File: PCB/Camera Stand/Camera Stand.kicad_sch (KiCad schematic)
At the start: 6 parts, among them J2 HMC5883L, J3 Motor Drive, J4 Keypad 4x4, J9 GPS Module, M1 Motor_Servo, U1 NRF24L01

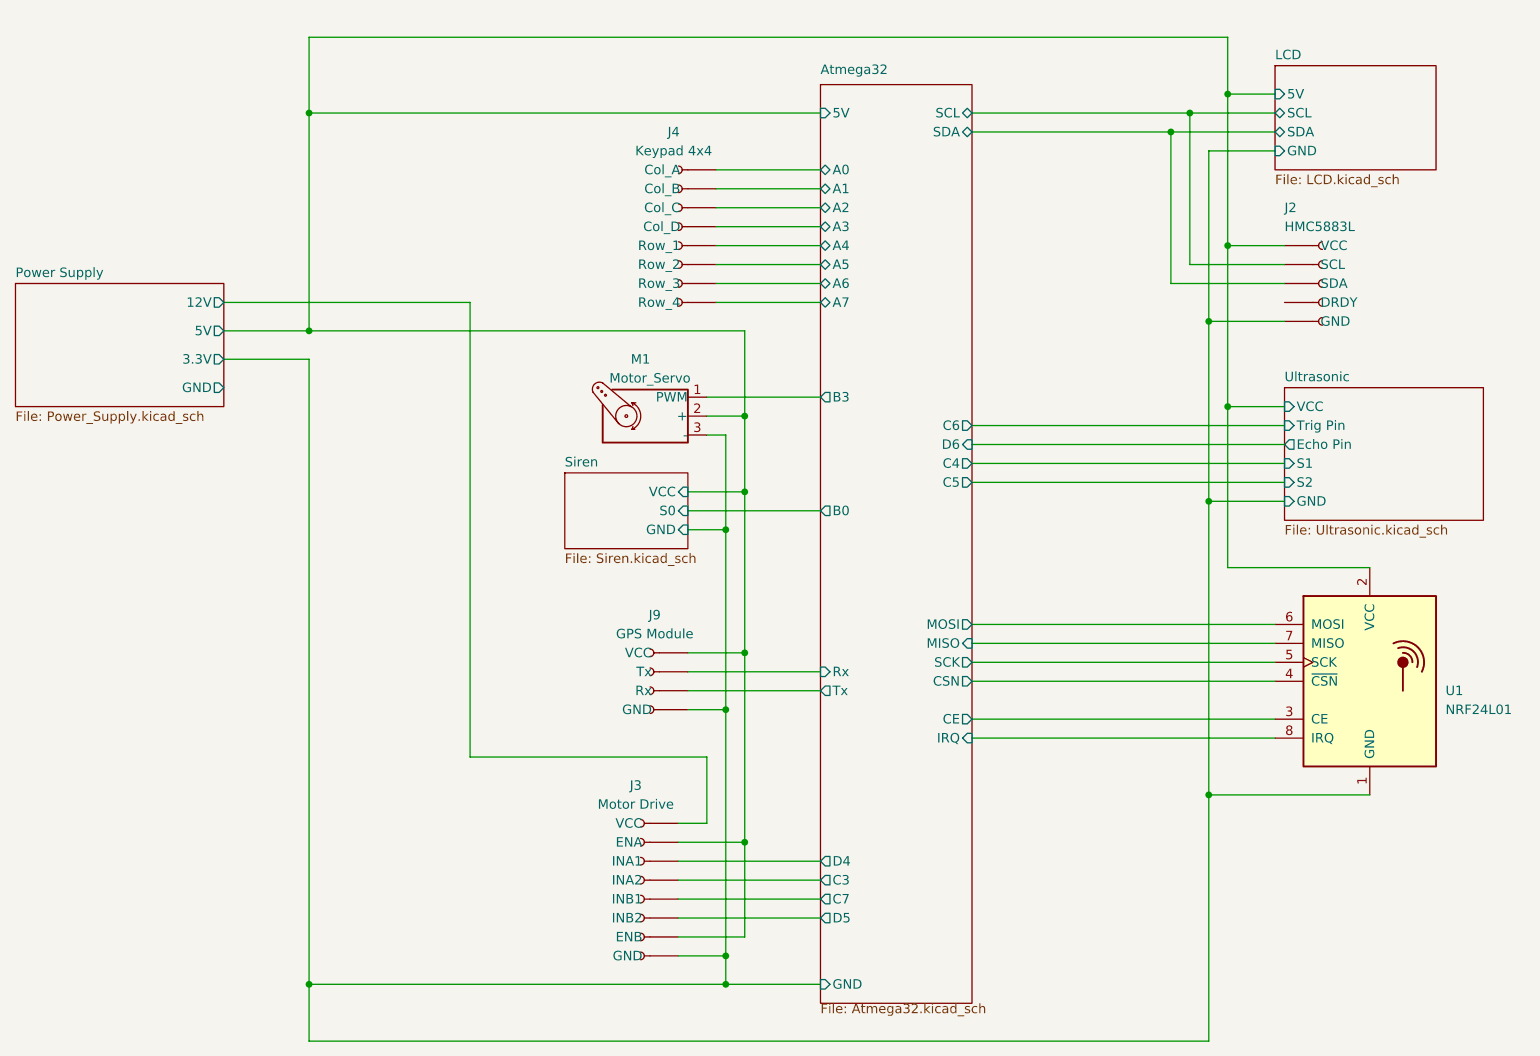
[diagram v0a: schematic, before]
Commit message: 3.3v error in PCB
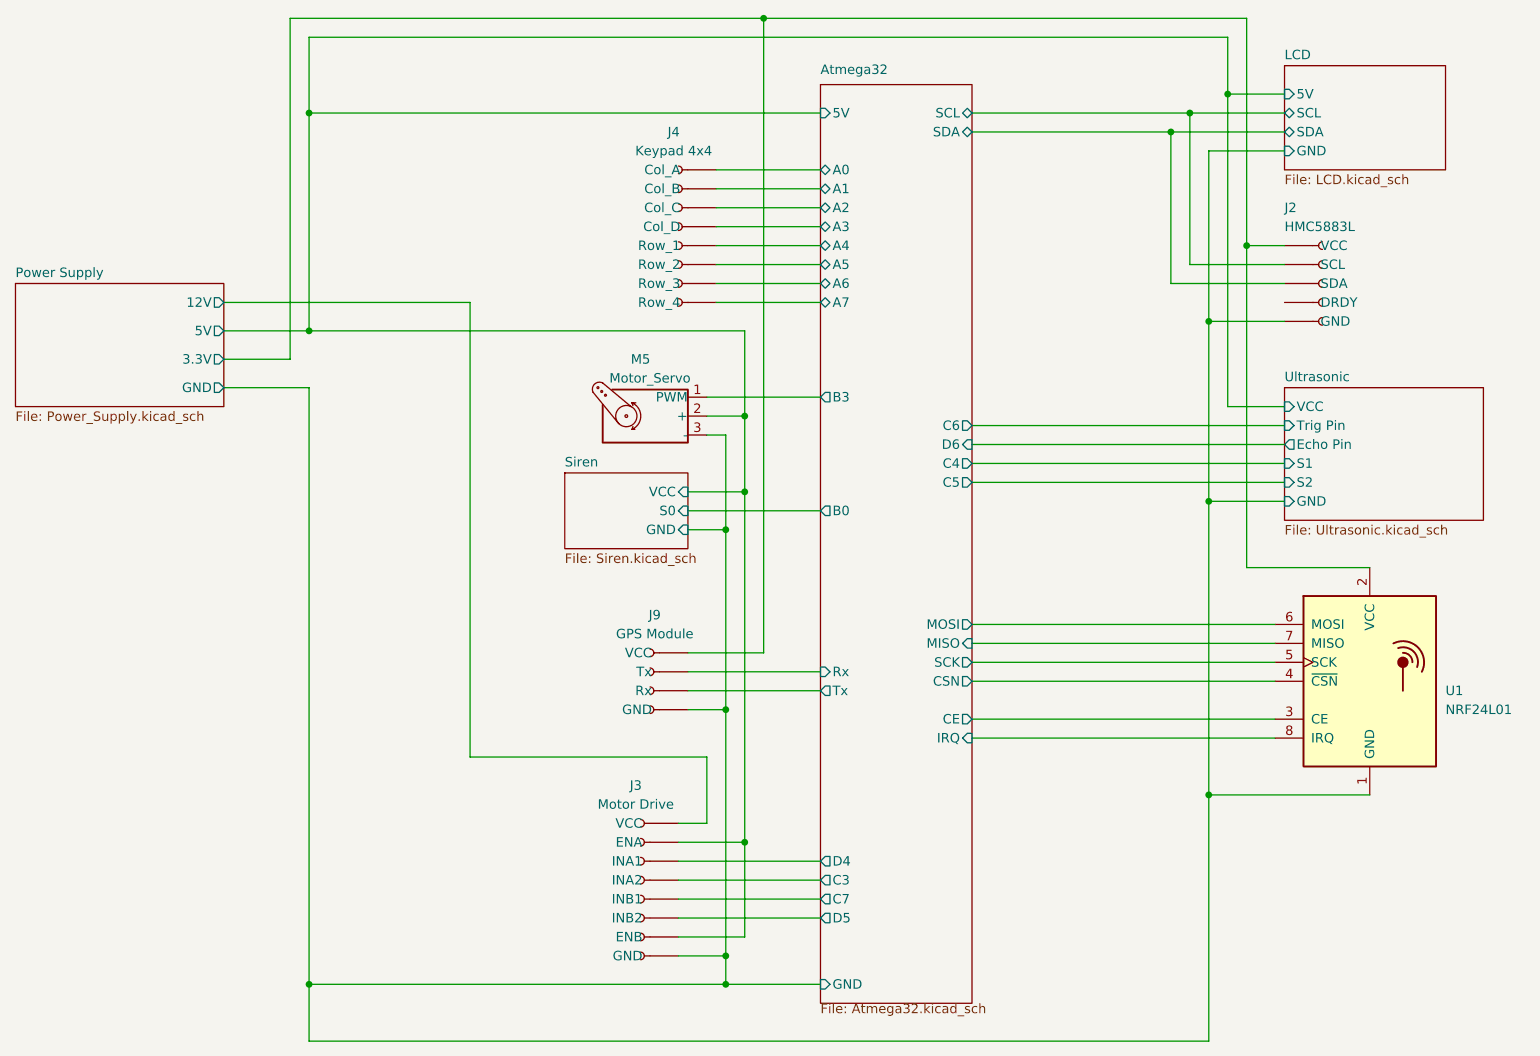
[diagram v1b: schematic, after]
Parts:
- renumbered M1 to M5
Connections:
- net Atmega32/5V: no longer J2.1 (VCC), J9.1 (VCC), U1.2 (VCC)
- new net Power Supply/3.3V: J2.1 (VCC), J9.1 (VCC), U1.2 (VCC)
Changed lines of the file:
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@@
   (junction (at 146.05 82.55) (diameter 0) (color 0 0 0 0)
   )
-  (junction (at 210.82 71.12) (diameter 0) (color 0 0 0 0)
-  )
   (junction (at 208.28 59.69) (diameter 0) (color 0 0 0 0)
   )
-  (junction (at 210.82 49.53) (diameter 0) (color 0 0 0 0)
-  )
-  (junction (at 146.05 104.14) (diameter 0) (color 0 0 0 0)
+  (junction (at 148.59 19.05) (diameter 0) (color 0 0 0 0)
   )
   (junction (at 87.63 148.59) (diameter 0) (color 0 0 0 0)
@@
   (junction (at 87.63 31.75) (diameter 0) (color 0 0 0 0)
   )
+  (junction (at 213.36 49.53) (diameter 0) (color 0 0 0 0)
+  )
   (junction (at 143.51 111.76) (diameter 0) (color 0 0 0 0)
   )
@@
     (stroke (width 0) (type default) (color 0 0 0 0))
   )
-  (wire (pts (xy 203.2 34.29) (xy 217.17 34.29))
+  (wire (pts (xy 203.2 34.29) (xy 218.44 34.29))
     (stroke (width 0) (type default) (color 0 0 0 0))
   )
@@
     (stroke (width 0) (type default) (color 0 0 0 0))
   )
-  (wire (pts (xy 208.28 36.83) (xy 217.17 36.83))
+  (wire (pts (xy 208.28 36.83) (xy 218.44 36.83))
     (stroke (width 0) (type default) (color 0 0 0 0))
   )
@@
     (stroke (width 0) (type default) (color 0 0 0 0))
   )
+  (wire (pts (xy 213.36 19.05) (xy 213.36 49.53))
+    (stroke (width 0) (type default) (color 0 0 0 0))
+  )
+  (wire (pts (xy 213.36 49.53) (xy 213.36 92.71))
+    (stroke (width 0) (type default) (color 0 0 0 0))
+  )
   (wire (pts (xy 208.28 123.19) (xy 208.28 83.82))
     (stroke (width 0) (type default) (color 0 0 0 0))
@@
     (stroke (width 0) (type default) (color 0 0 0 0))
   )
-  (wire (pts (xy 210.82 49.53) (xy 210.82 29.21))
+  (wire (pts (xy 210.82 29.21) (xy 210.82 71.12))
     (stroke (width 0) (type default) (color 0 0 0 0))
   )
@@
     (stroke (width 0) (type default) (color 0 0 0 0))
   )
-  (wire (pts (xy 76.2 64.77) (xy 87.63 64.77))
-    (stroke (width 0) (type default) (color 0 0 0 0))
-  )
   (wire (pts (xy 140.97 118.11) (xy 140.97 127))
     (stroke (width 0) (type default) (color 0 0 0 0))
@@
     (stroke (width 0) (type default) (color 0 0 0 0))
   )
-  (wire (pts (xy 146.05 82.55) (xy 146.05 104.14))
+  (wire (pts (xy 146.05 82.55) (xy 146.05 129.54))
     (stroke (width 0) (type default) (color 0 0 0 0))
   )
@@
     (stroke (width 0) (type default) (color 0 0 0 0))
   )
-  (wire (pts (xy 205.74 31.75) (xy 217.17 31.75))
+  (wire (pts (xy 87.63 68.58) (xy 87.63 148.59))
+    (stroke (width 0) (type default) (color 0 0 0 0))
+  )
+  (wire (pts (xy 205.74 31.75) (xy 218.44 31.75))
+    (stroke (width 0) (type default) (color 0 0 0 0))
+  )
+  (wire (pts (xy 148.59 19.05) (xy 148.59 104.14))
     (stroke (width 0) (type default) (color 0 0 0 0))
   )
@@
     (stroke (width 0) (type default) (color 0 0 0 0))
   )
+  (wire (pts (xy 76.2 64.77) (xy 85.09 64.77))
+    (stroke (width 0) (type default) (color 0 0 0 0))
+  )
   (wire (pts (xy 146.05 72.39) (xy 146.05 82.55))
     (stroke (width 0) (type default) (color 0 0 0 0))
@@
     (stroke (width 0) (type default) (color 0 0 0 0))
   )
-  (wire (pts (xy 210.82 71.12) (xy 210.82 92.71))
-    (stroke (width 0) (type default) (color 0 0 0 0))
-  )
   (wire (pts (xy 137.16 137.16) (xy 156.21 137.16))
     (stroke (width 0) (type default) (color 0 0 0 0))
   )
-  (wire (pts (xy 138.43 104.14) (xy 146.05 104.14))
+  (wire (pts (xy 138.43 104.14) (xy 148.59 104.14))
     (stroke (width 0) (type default) (color 0 0 0 0))
   )
@@
     (stroke (width 0) (type default) (color 0 0 0 0))
   )
+  (wire (pts (xy 85.09 19.05) (xy 148.59 19.05))
+    (stroke (width 0) (type default) (color 0 0 0 0))
+  )
   (wire (pts (xy 176.53 105.41) (xy 217.17 105.41))
     (stroke (width 0) (type default) (color 0 0 0 0))
@@
     (stroke (width 0) (type default) (color 0 0 0 0))
   )
-  (wire (pts (xy 229.87 92.71) (xy 210.82 92.71))
+  (wire (pts (xy 229.87 92.71) (xy 213.36 92.71))
     (stroke (width 0) (type default) (color 0 0 0 0))
   )
@@
     (stroke (width 0) (type default) (color 0 0 0 0))
   )
-  (wire (pts (xy 210.82 71.12) (xy 210.82 49.53))
-    (stroke (width 0) (type default) (color 0 0 0 0))
-  )
   (wire (pts (xy 176.53 76.2) (xy 218.44 76.2))
     (stroke (width 0) (type default) (color 0 0 0 0))
@@
     (stroke (width 0) (type default) (color 0 0 0 0))
   )
-  (wire (pts (xy 210.82 29.21) (xy 217.17 29.21))
+  (wire (pts (xy 210.82 29.21) (xy 218.44 29.21))
     (stroke (width 0) (type default) (color 0 0 0 0))
   )
@@
     (stroke (width 0) (type default) (color 0 0 0 0))
   )
+  (wire (pts (xy 148.59 19.05) (xy 213.36 19.05))
+    (stroke (width 0) (type default) (color 0 0 0 0))
+  )
+  (wire (pts (xy 85.09 64.77) (xy 85.09 19.05))
+    (stroke (width 0) (type default) (color 0 0 0 0))
+  )
   (wire (pts (xy 138.43 106.68) (xy 156.21 106.68))
     (stroke (width 0) (type default) (color 0 0 0 0))
   )
+  (wire (pts (xy 76.2 68.58) (xy 87.63 68.58))
+    (stroke (width 0) (type default) (color 0 0 0 0))
+  )
   (wire (pts (xy 143.51 144.78) (xy 143.51 148.59))
     (stroke (width 0) (type default) (color 0 0 0 0))
   )
-  (wire (pts (xy 218.44 49.53) (xy 210.82 49.53))
+  (wire (pts (xy 213.36 49.53) (xy 218.44 49.53))
     (stroke (width 0) (type default) (color 0 0 0 0))
   )
@@
     (stroke (width 0) (type default) (color 0 0 0 0))
   )
-  (wire (pts (xy 87.63 64.77) (xy 87.63 148.59))
-    (stroke (width 0) (type default) (color 0 0 0 0))
-  )
   (wire (pts (xy 176.53 107.95) (xy 217.17 107.95))
-    (stroke (width 0) (type default) (color 0 0 0 0))
-  )
-  (wire (pts (xy 146.05 104.14) (xy 146.05 129.54))
     (stroke (width 0) (type default) (color 0 0 0 0))
   )
   (symbol (lib_id "Motor:Motor_Servo") (at 133.35 72.39 0) (mirror y) (unit 1)
     (in_bom yes) (on_board yes)
-    (property "Reference" "M1" (id 0) (at 132.08 64.77 0))
+    (property "Reference" "M5" (id 0) (at 132.08 64.77 0))
     (property "Value" "Motor_Servo" (id 1) (at 133.35 67.31 0))
     (property "Footprint" "Connector_PinHeader_2.54mm:PinHeader_1x03_P2.54mm_Vertical" (id 2) (at 133.35 77.216 0)
@@
     )
   )
-  (sheet (at 217.17 25.4) (size 21.59 13.97) (fields_autoplaced)
+  (sheet (at 218.44 25.4) (size 21.59 13.97) (fields_autoplaced)
     (stroke (width 0.1524) (type solid) (color 0 0 0 0))
     (fill (color 0 0 0 0.0000))
-    (property "Sheet name" "LCD" (id 0) (at 217.17 24.6884 0)
+    (property "Sheet name" "LCD" (id 0) (at 218.44 24.6884 0)
       (effects (font (size 1.27 1.27)) (justify left bottom))
     )
-    (property "Sheet file" "LCD.kicad_sch" (id 1) (at 217.17 39.9546 0)
+    (property "Sheet file" "LCD.kicad_sch" (id 1) (at 218.44 39.9546 0)
       (effects (font (size 1.27 1.27)) (justify left top))
     )
-    (pin "SCL" bidirectional (at 217.17 31.75 180)
-      (effects (font (size 1.27 1.27)) (justify left))
-    )
-    (pin "SDA" bidirectional (at 217.17 34.29 180)
-      (effects (font (size 1.27 1.27)) (justify left))
-    )
-    (pin "GND" input (at 217.17 36.83 180)
-      (effects (font (size 1.27 1.27)) (justify left))
-    )
-    (pin "5V" input (at 217.17 29.21 180)
+    (pin "SCL" bidirectional (at 218.44 31.75 180)
+      (effects (font (size 1.27 1.27)) (justify left))
+    )
+    (pin "SDA" bidirectional (at 218.44 34.29 180)
+      (effects (font (size 1.27 1.27)) (justify left))
+    )
+    (pin "GND" input (at 218.44 36.83 180)
+      (effects (font (size 1.27 1.27)) (justify left))
+    )
+    (pin "5V" input (at 218.44 29.21 180)
       (effects (font (size 1.27 1.27)) (justify left))
     )
@@
     )
     (path "/87422020-02e0-4c0f-a285-e763ed24a836/067d786d-63e8-42d4-9057-5db31f0b128f"
-      (reference "K?") (unit 1) (value "Relay") (footprint "Relay_THT:Relay_SPDT_Finder_36.11")
+      (reference "K1") (unit 1) (value "Relay") (footprint "Relay_THT:Relay_SPDT_Finder_36.11")
     )
     (path "/87422020-02e0-4c0f-a285-e763ed24a836/01eff278-24f6-440c-a589-37d8d7c761d3"
@@
     )
     (path "/13635d61-fb4b-4c1a-b172-4cf2222e0dab"
-      (reference "M1") (unit 1) (value "Motor_Servo") (footprint "Connector_PinHeader_2.54mm:PinHeader_1x03_P2.54mm_Vertical")
+      (reference "M5") (unit 1) (value "Motor_Servo") (footprint "Connector_PinHeader_2.54mm:PinHeader_1x03_P2.54mm_Vertical")
     )
     (path "/87422020-02e0-4c0f-a285-e763ed24a836/9c778911-6cd8-4b64-bce4-d0bbb7572602"
